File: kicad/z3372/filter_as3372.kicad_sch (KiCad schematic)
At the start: 69 parts, among them Q1 MMBT3904, Q2 MMBT3904, U11 DG442xY, U18 NE5532, U19 L79L05_TO92, U5 TL072, U6 AS3360-Audio, U8 AS3372

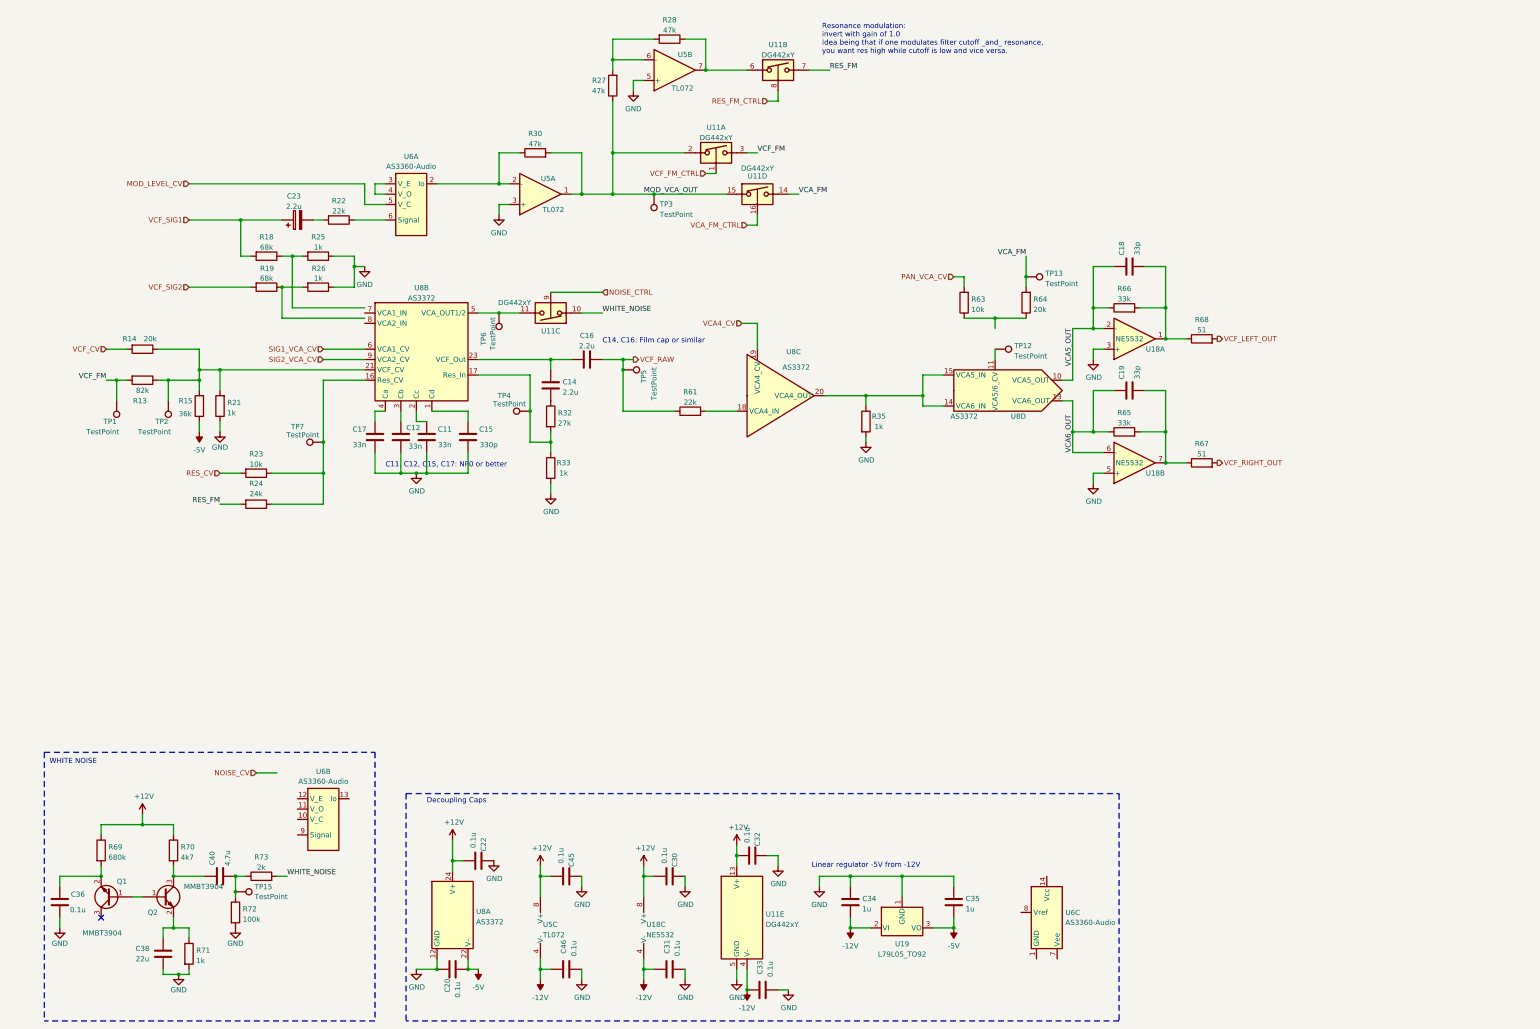
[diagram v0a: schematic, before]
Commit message: schematic done.  some values need tweaking.  design review still needed
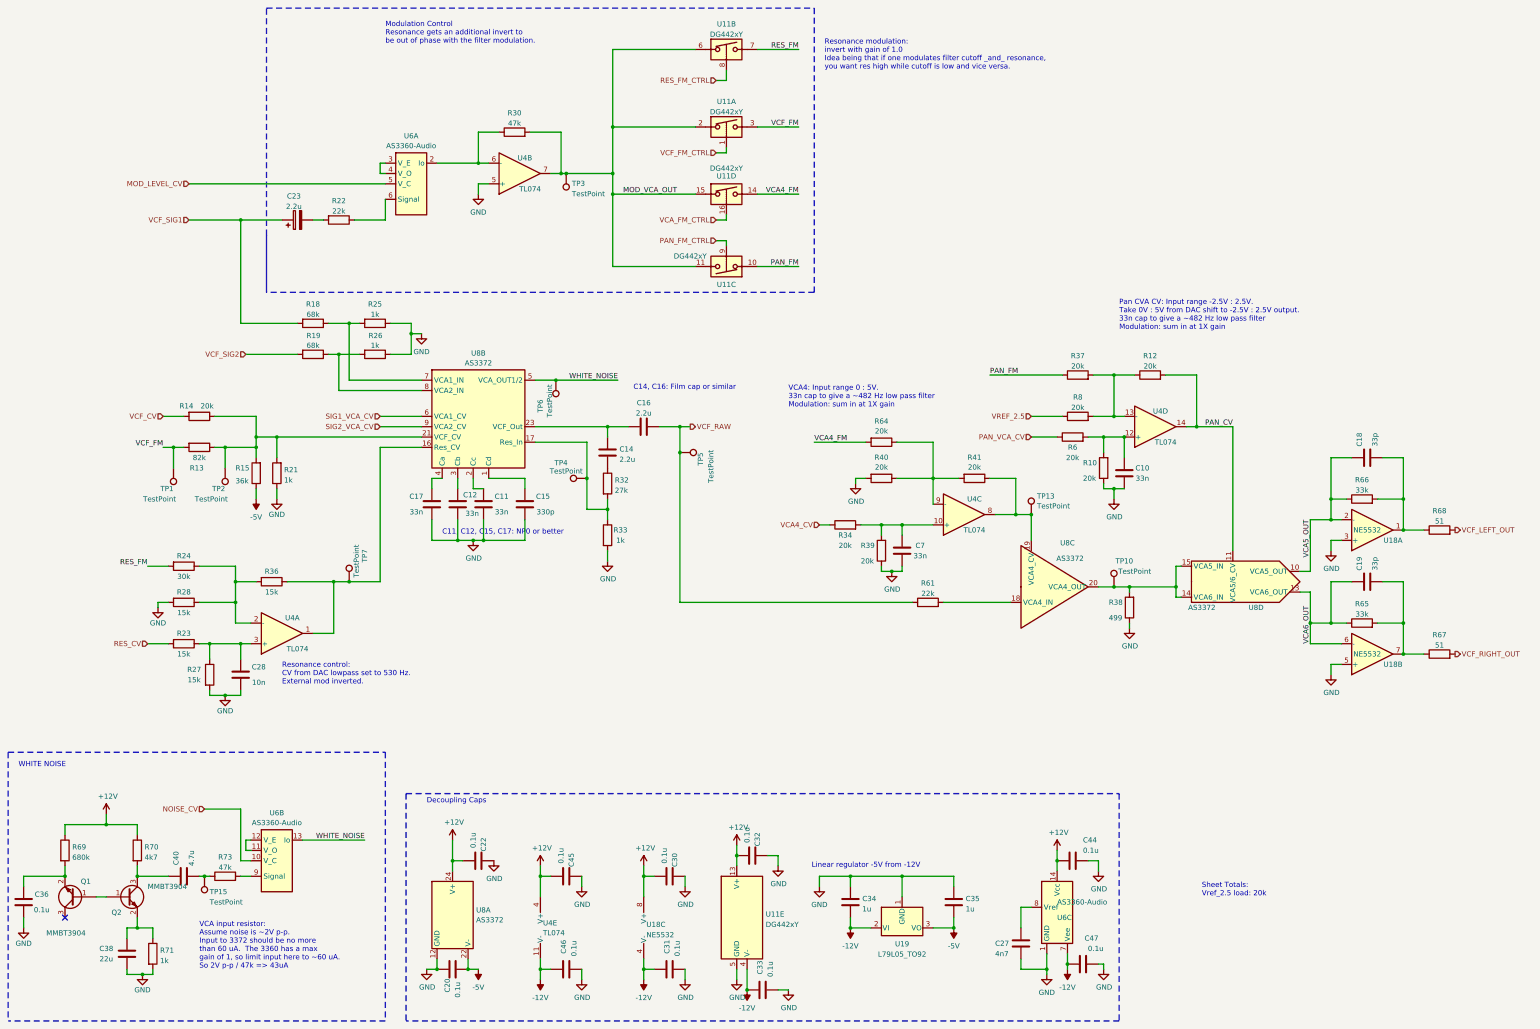
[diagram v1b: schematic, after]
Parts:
- removed R35: 1k, Resistor_SMD:R_0603_1608Metric, symbol Device:R
- removed R63: 10k, Resistor_SMD:R_0603_1608Metric, symbol Device:R
- removed R72: 100k, Resistor_SMD:R_0402_1005Metric, symbol Device:R
- removed TP12: TestPoint, TestPoint:TestPoint_Pad_2.0x2.0mm, symbol Connector:TestPoint
- removed U5: TL072, Package_SO:SOIC-8_3.9x4.9mm_P1.27mm, symbol Amplifier_Operational:TL072
- added C10, C7: 33n, Capacitor_SMD:C_0603_1608Metric, symbol Device:C
- added C27: 4n7, Capacitor_SMD:C_0805_2012Metric, symbol Device:C
- added C28: 10n, Capacitor_SMD:C_0603_1608Metric, symbol Device:C
- added C44, C47: 0.1u, Capacitor_SMD:C_0603_1608Metric, symbol Device:C
- added R10, R12, R34, R37, R39, R40, R41, R6, R8: 20k, Resistor_SMD:R_0603_1608Metric, symbol Device:R
- added R36: 15k, Resistor_SMD:R_0603_1608Metric, symbol Device:R
- added R38: 499, Resistor_SMD:R_0603_1608Metric, symbol Device:R
- added TP10: TestPoint, TestPoint:TestPoint_Pad_2.0x2.0mm, symbol Connector:TestPoint
- added U4: TL074, symbol Amplifier_Operational:TL074
- R23: value 10k -> 15k; LCSC Part C25804 -> (none)
- R24: value 24k -> 30k; LCSC Part C23352 -> (none)
- R27, R28: value 47k -> 15k; LCSC Part C25819 -> (none)
- R64: LCSC Part C4184 -> (none)
- R73: value 2k -> 47k; LCSC Part C22975 -> C25819
- U8: symbol as3372_lib:AS3372 -> z3372_lib:AS3372
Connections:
- net +12V: now also U6.14 (Vcc), C44.2, U4.4 (V+)
- net -12V: now also U6.7 (Vee), C47.1, U4.11 (V-)
- net GND: now also R27.2, R28.2, U6.1 (GND), C10.2, C27.2, C28.2, C44.1, C47.2, C7.2, R10.1, R38.1, R39.1, R40.2, U4.5 (+)
- net MOD_VCA_OUT: now also U11.11, U11.6, U4.7; no longer R27.1
- net NOISE_CV: now also U6.10 (V_C)
- net PAN_VCA_CV: now also R6.1
- net VCA4_CV: now also R34.1; no longer U8.19 (VCA4_CV)
- net WHITE_NOISE: now also TP6.1, U6.13 (Io), U8.5 (VCA_OUT1/2); no longer R73.2, U11.10
- net at R64.1: now also R40.1, R41.2, U4.9 (-)
- net at R30.1, U6.2 (Io): now also U4.6 (-)
- net at U6.11 (V_O): now also U6.12 (V_E)
- net at U6.9 (Signal): now also R73.2
- net at U6.8 (Vref): now also C27.1
- net at R28.1: now also R24.1, R36.2, U4.2 (-); no longer U11.6
- net at R19.1, R26.2: now also U8.8 (VCA2_IN)
- net at R18.1, R25.2: now also U8.7 (VCA1_IN)
- net PAN_CV: now reaches U8.11 (VCA5/6_CV)
- net PAN_CV: now also R12.2, U4.14
- net at U8.14 (VCA6_IN), U8.15 (VCA5_IN), U8.20 (VCA4_OUT): now also R38.2, TP10.1
- net at TP7.1, U8.16 (Res_CV): now also R36.1, U4.1; no longer R23.1, R24.1
- net NOISE_CTRL renamed PAN_FM_CTRL
- net VCA_FM renamed VCA4_FM
- net VCA4_FM: no longer TP13.1
- new net: R12.1, R37.2, R8.2, U4.13 (-)
- new net: C10.1, R10.2, R6.2, U4.12 (+)
- new net: C7.1, R34.2, R39.2, U4.10 (+)
- new net: R41.1, TP13.1, U4.8, U8.19 (VCA4_CV)
- new net: C28.1, R23.1, R27.1, U4.3 (+)
- new net PAN_FM: R37.1, U11.10
- new net VREF_2.5: R8.1
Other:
- note added: "Modulation Control Resonance gets an additional invert to be out of phase with the filter modulation."
- note added: "Pan CVA CV: Input range -2.5V : 2.5V. Take 0V : 5V from DAC shift to -2.5V : 2.5V output. 33n cap to give a ~482 Hz low pass filter Modulation: sum in at 1X gain"
- note added: "Resonance control: CV from DAC lowpass set to 530 Hz. External mod inverted."
- note added: "Sheet Totals: Vref_2.5 load: 20k"
- note added: "VCA input resistor: Assume noise is ~2V p-p. Input to 3372 should be no more than 60 uA. The 3360 has a max gain of 1, so limit input here to ~60 uA. So 2V p-p / 47k => 43uA"
- note added: "VCA4: Input range 0 : 5V. 33n cap to give a ~482 Hz low pass filter Modulation: sum in at 1X gain"
- moved on the sheet: C11, C12, C14, C15, C16, C17, C18, C19, C36, C38, C40, Q1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

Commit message: review underway for AS3372
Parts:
- added C8: 0.1u, Capacitor_SMD:C_0603_1608Metric, symbol Device:C
- added R42: 2k, Resistor_SMD:R_0603_1608Metric, symbol Device:R
- R13: value 82k -> 36k; LCSC Part C23254 -> C23147
- R14: value 20k -> 18k; LCSC Part C4184 -> (none)
- R73: value 47k -> 36k; LCSC Part C25819 -> C23147
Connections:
- net GND: now also C8.2
- net VCF_CV: now also R42.2; no longer R14.2
- new net: C8.1, R14.2, R42.1
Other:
- note added: "VCF Control: VCF from DAC has 2k/0.1u RC filter @ 800 Hz. External mod has slightly less pull at 36k versus DAC at 20k effective."
- moved on the sheet: R13, R14, TP1, TP2

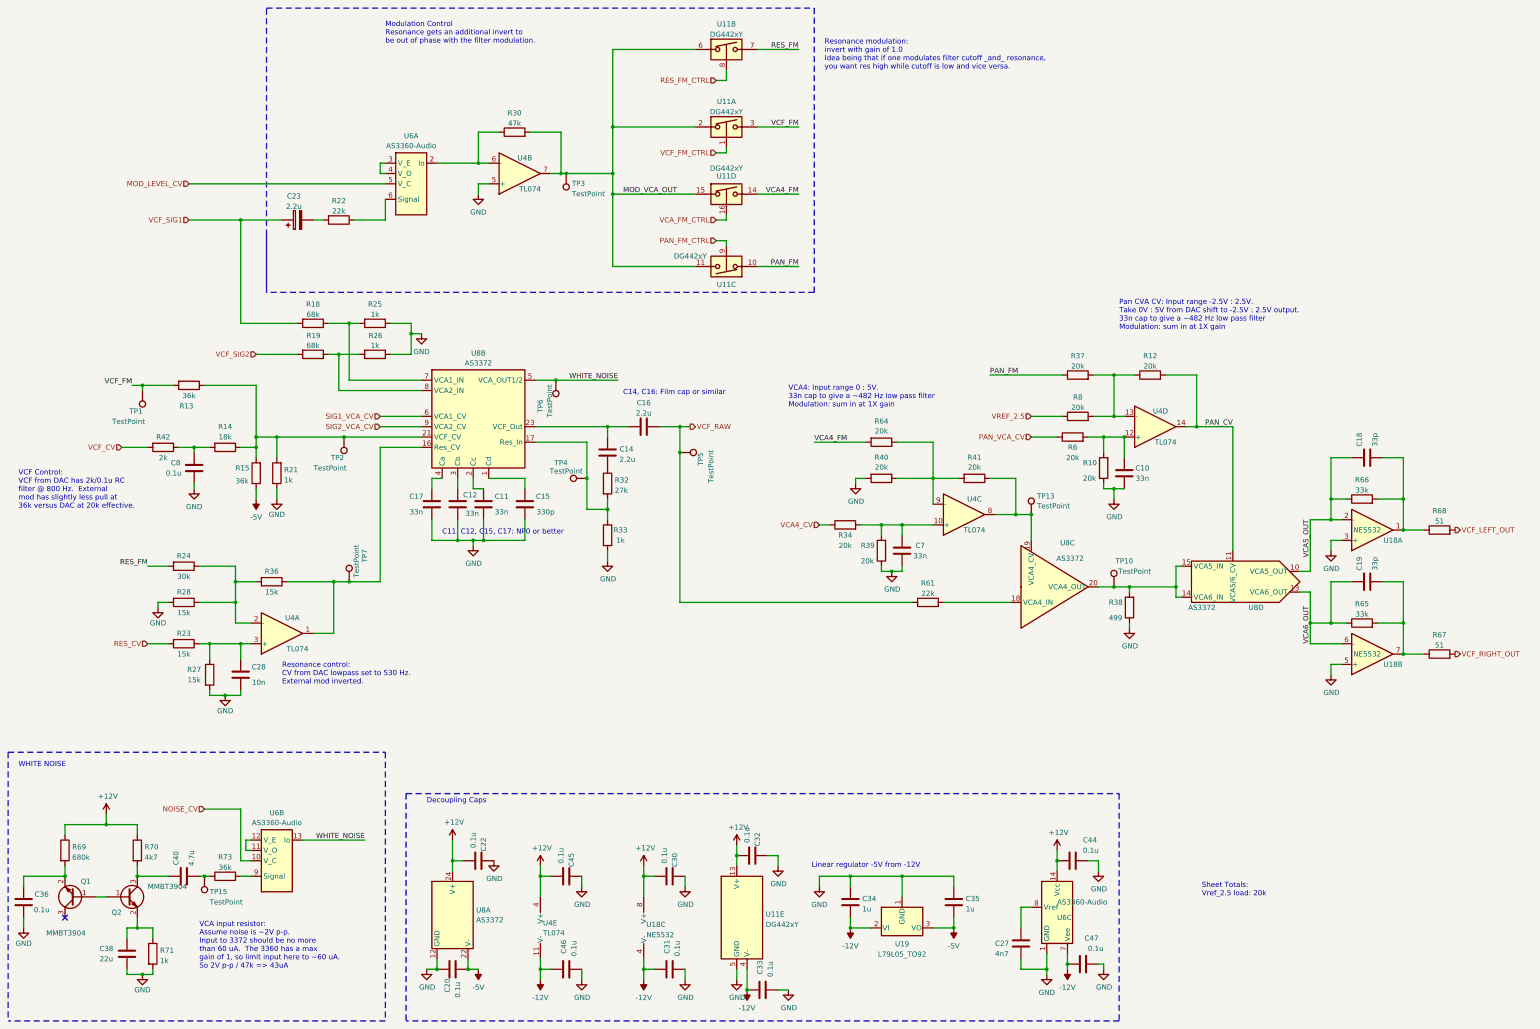
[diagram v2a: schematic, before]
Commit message: schematic completed, working on place and route
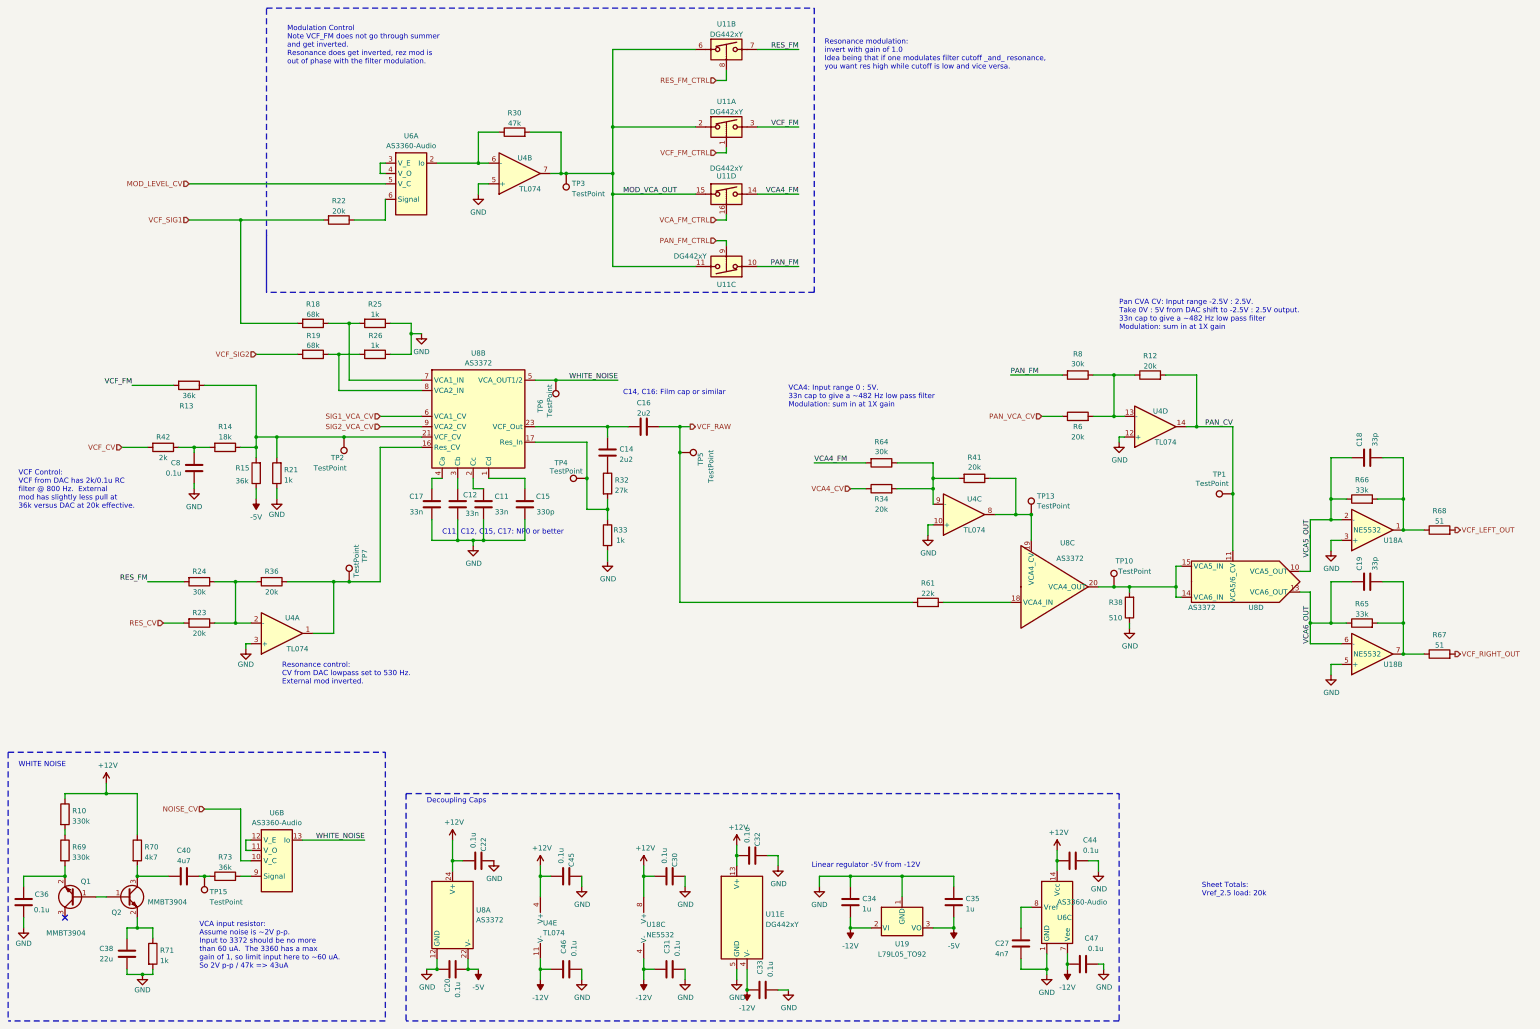
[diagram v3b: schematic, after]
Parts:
- removed C10, C7: 33n, Capacitor_SMD:C_0603_1608Metric, symbol Device:C
- removed C23: 2.2u, Capacitor_THT:CP_Radial_D4.0mm_P1.50mm, symbol Device:C_Polarized
- removed C28: 10n, Capacitor_SMD:C_0603_1608Metric, symbol Device:C
- removed R27, R28: 15k, Resistor_SMD:R_0603_1608Metric, symbol Device:R
- removed R37, R39, R40: 20k, Resistor_SMD:R_0603_1608Metric, symbol Device:R
- C14, C16: value 2.2u -> 2u2
- C15: footprint Capacitor_SMD:C_0805_2012Metric -> Capacitor_SMD:C_0603_1608Metric; LCSC Part C694185 -> C1664
- C27: footprint Capacitor_SMD:C_0805_2012Metric -> Capacitor_SMD:C_0603_1608Metric; LCSC Part (none) -> C53987
- C40: value 4.7u -> 4u7
- R10: value 20k -> 330k; LCSC Part C4184 -> C23137
- R14: LCSC Part (none) -> C25810
- R22: value 22k -> 20k; LCSC Part C31850 -> C4184
- R23, R36: value 15k -> 20k; LCSC Part (none) -> C4184
- R24: LCSC Part (none) -> C22984
- R38: value 499 -> 510; LCSC Part (none) -> C23193
- R42: LCSC Part (none) -> C22975
- R64: value 20k -> 30k; LCSC Part (none) -> C22984
- R67, R68: LCSC Part (none) -> C23197
- R69: value 680k -> 330k; LCSC Part C25822 -> C23137
- R8: value 20k -> 30k; LCSC Part C4184 -> C22984
- U4: footprint (none) -> Package_SO:TSSOP-14_4.4x5mm_P0.65mm; LCSC Part (none) -> C96507
- U6: footprint (none) -> Package_SO:SOIC-14_3.9x8.7mm_P1.27mm
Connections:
- net VREF_2.5 is gone; now on an unnamed net: R8.1
- net +12V: now also R10.1; no longer R69.1
- net GND: now also U4.10 (+), U4.12 (+), U4.3 (+); no longer R10.1
- net PAN_CV: now also TP1.1
- net PAN_FM: now also R8.2
- net VCF_FM: no longer TP1.1
- net VCF_SIG1: now also R22.2
- net at R41.2, R64.1, U4.9 (-): now also R34.2
- net at R12.1, U4.13 (-): now also R6.2; no longer R8.2
- net at R24.1, R36.2, U4.2 (-): now also R23.1
- new net: R10.2, R69.1
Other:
- note added: "Modulation Control Note VCF_FM does not go through summer and get inverted. Resonance does get inverted, rez mod is out of phase with the filter modulation."
- note removed: "Modulation Control Resonance gets an additional invert to be out of phase with the filter modulation."
- moved on the sheet: R23, R24, R34, R6, R64

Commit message: placement improvements
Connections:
- net MOD_LEVEL_CV: now also U6.10 (V_C); no longer U6.5 (V_C)
- net MOD_VCA_OUT: now also U11.15, U11.6; no longer U11.15, U11.6
- net NOISE_CV: now also U6.5 (V_C); no longer U6.10 (V_C)
- net RES_FM: now also U11.14; no longer U11.7
- net RES_FM_CTRL: now also U11.16; no longer U11.8
- net VCA4_FM: now also U11.7; no longer U11.14
- net VCA_FM_CTRL: now also U11.8; no longer U11.16
- net WHITE_NOISE: now also U6.2 (Io); no longer U6.13 (Io)
- net at R73.2: now also U6.6 (Signal); no longer U6.9 (Signal)
- net at R30.1, U4.6 (-): now also U6.13 (Io); no longer U6.2 (Io)
- net at R22.1: now also U6.9 (Signal); no longer U6.6 (Signal)
- new net: U6.3 (V_E), U6.4 (V_O)
- new net: U6.11 (V_O), U6.12 (V_E)
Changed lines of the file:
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@@
     )
   )
-  (symbol (lib_id "z3372_lib:AS3360-Audio") (at 85.09 220.98 0) (unit 2)
+  (symbol (lib_id "z3372_lib:AS3360-Audio") (at 85.09 220.98 0) (unit 1)
     (in_bom yes) (on_board yes) (dnp no) (fields_autoplaced)
     (property "Reference" "U6" (at 85.09 210.4857 0)
@@
       (project "z3372"
         (path "/7079bdb0-a00e-4bac-b257-cbcf2c91bbd6/06519ee5-e3f7-4c1d-97d6-a8703fead30d"
-          (reference "U6") (unit 2)
+          (reference "U6") (unit 1)
         )
       )
@@
     )
   )
-  (symbol (lib_id "Analog_Switch:DG442xY") (at 195.58 22.86 0) (unit 2)
+  (symbol (lib_id "Analog_Switch:DG442xY") (at 195.58 22.86 0) (unit 4)
     (in_bom yes) (on_board yes) (dnp no) (fields_autoplaced)
     (property "Reference" "U11" (at 195.58 16.6202 0)
@@
       (project "z3372"
         (path "/7079bdb0-a00e-4bac-b257-cbcf2c91bbd6/06519ee5-e3f7-4c1d-97d6-a8703fead30d"
-          (reference "U11") (unit 2)
+          (reference "U11") (unit 4)
         )
       )
@@
     )
   )
-  (symbol (lib_id "z3372_lib:AS3360-Audio") (at 118.11 54.61 0) (unit 1)
+  (symbol (lib_id "z3372_lib:AS3360-Audio") (at 118.11 54.61 0) (unit 2)
     (in_bom yes) (on_board yes) (dnp no) (fields_autoplaced)
     (property "Reference" "U6" (at 118.11 44.1157 0)
@@
       (project "z3372"
         (path "/7079bdb0-a00e-4bac-b257-cbcf2c91bbd6/06519ee5-e3f7-4c1d-97d6-a8703fead30d"
-          (reference "U6") (unit 1)
+          (reference "U6") (unit 2)
         )
       )
@@
     )
   )
-  (symbol (lib_id "Analog_Switch:DG442xY") (at 195.58 58.42 0) (unit 4)
+  (symbol (lib_id "Analog_Switch:DG442xY") (at 195.58 58.42 0) (unit 2)
     (in_bom yes) (on_board yes) (dnp no)
     (property "Reference" "U11" (at 195.58 53.975 0)
@@
       (project "z3372"
         (path "/7079bdb0-a00e-4bac-b257-cbcf2c91bbd6/06519ee5-e3f7-4c1d-97d6-a8703fead30d"
-          (reference "U11") (unit 4)
+          (reference "U11") (unit 2)
         )
       )
